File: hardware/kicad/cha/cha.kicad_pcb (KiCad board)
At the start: 4 copper layers, 173 x 134 mm, 138 parts, among them J1 AES_CHA, J2 PROG C, J3 PROG SM, J4 microSD, J5 Câble PROG-CHA, SW1 Retour menu, U1 AMS1117-3.3, U10 74AHCT1G32, U11 74LVC1G07, U12 iCE40HX4K-TQ144, U13 W25Q32JVSS, U14 AS4C32M16SB-6TIN, U15 iCE40HX4K-TQ144, U16 W25Q32JVSS, U17 IS61WV10248EDBLL-10TLI, U2 AP2112K-1.2, U3 74LVC16244A, U4 74LVC16244A, U5 74LVC16244A, U6 74LVC16244A, U7 74AHCT16244, U8 74AHCT16244, U9 74AHCT244, X1 25 MHz 3,3 V, X2 25 MHz 3,3 V

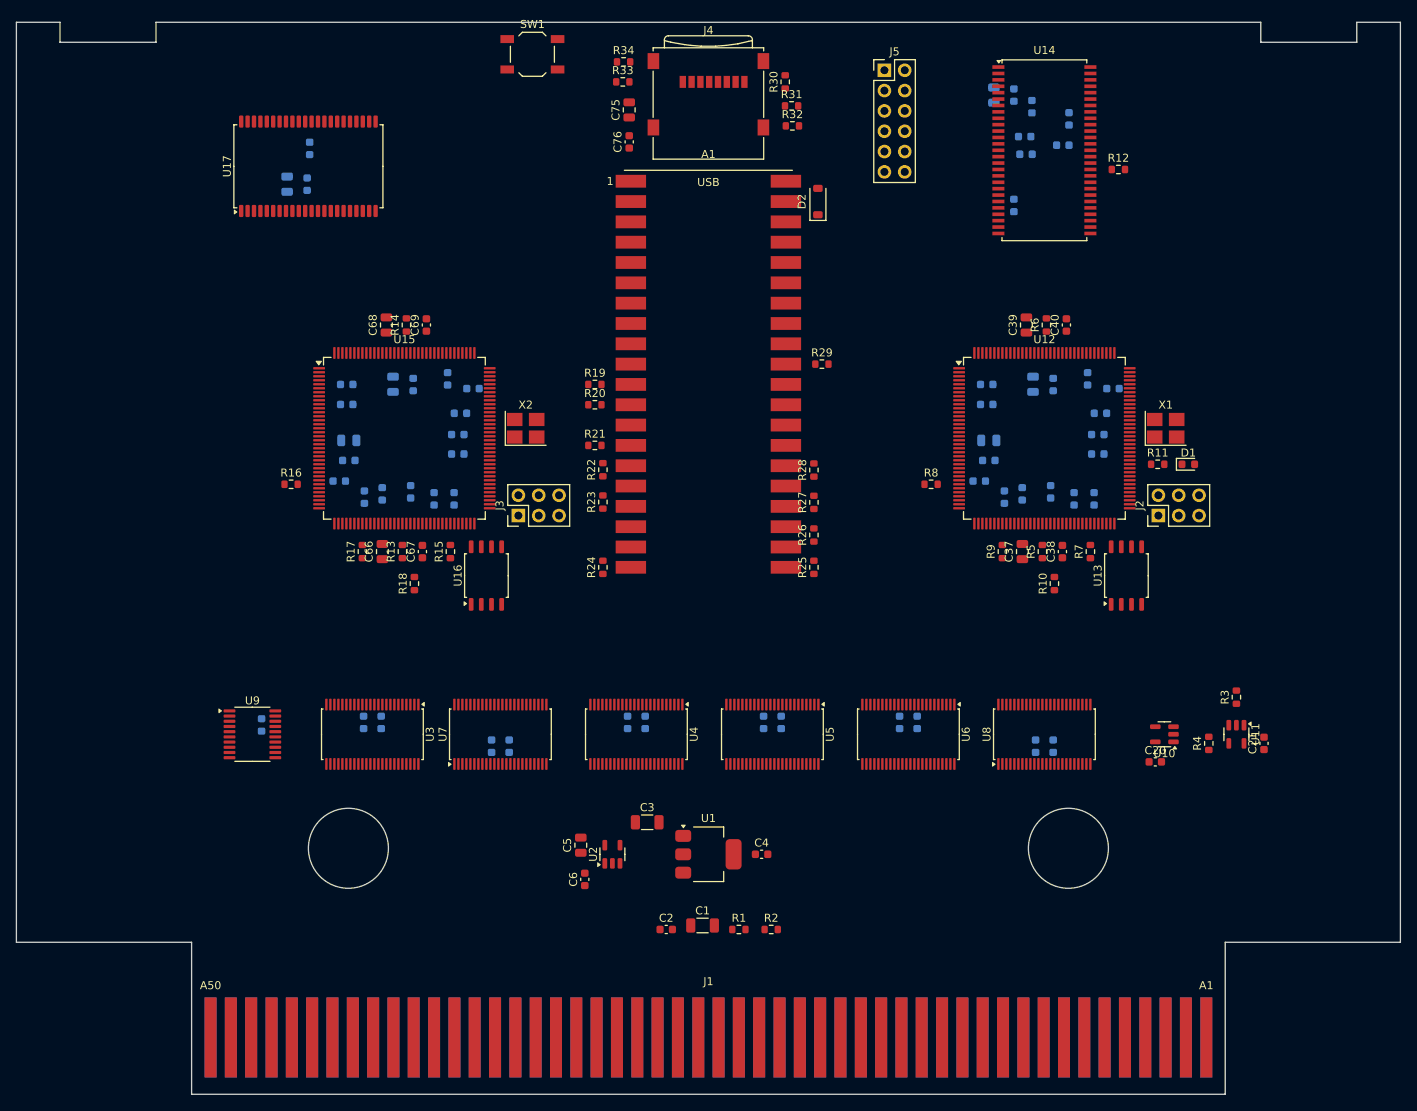
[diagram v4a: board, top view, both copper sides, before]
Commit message: PCB : 9 trous d'entretoise, vias vers les plans, zones interdites
- 9 trous M3 aux mêmes coordonnées sur PROG et CHA (H1-H9) pour relier
  les deux cartes par des entretoises ; 3,5 mm sans composant ni cuivre
  autour.
- Vias de raccordement aux plans (masse, +3V3) posés avant le routage
  pour chaque pastille CMS : au premier routage complet de la carte
  PROG, tous les signaux étaient routés et les 85 liaisons manquantes
  étaient toutes des raccordements aux plans.
- Zones interdites aux pistes autour des trous de la coque et des
  entretoises ; rétrécissement à 0,09 mm admis à l'entrée des broches.
- route.py : DRC par le module pcbnew (kicad-cli 7 n'en a pas), lecture
  de session corrigée.
- Pico descendu de 3 mm (chevauchait le lecteur microSD).

Co-Authored-By: Claude Opus 5.5 <noreply@anthropic.com>
Claude-Session: https://claude.ai/code/session_01WKfXP1YJ8otGxZ5dsY6Agh
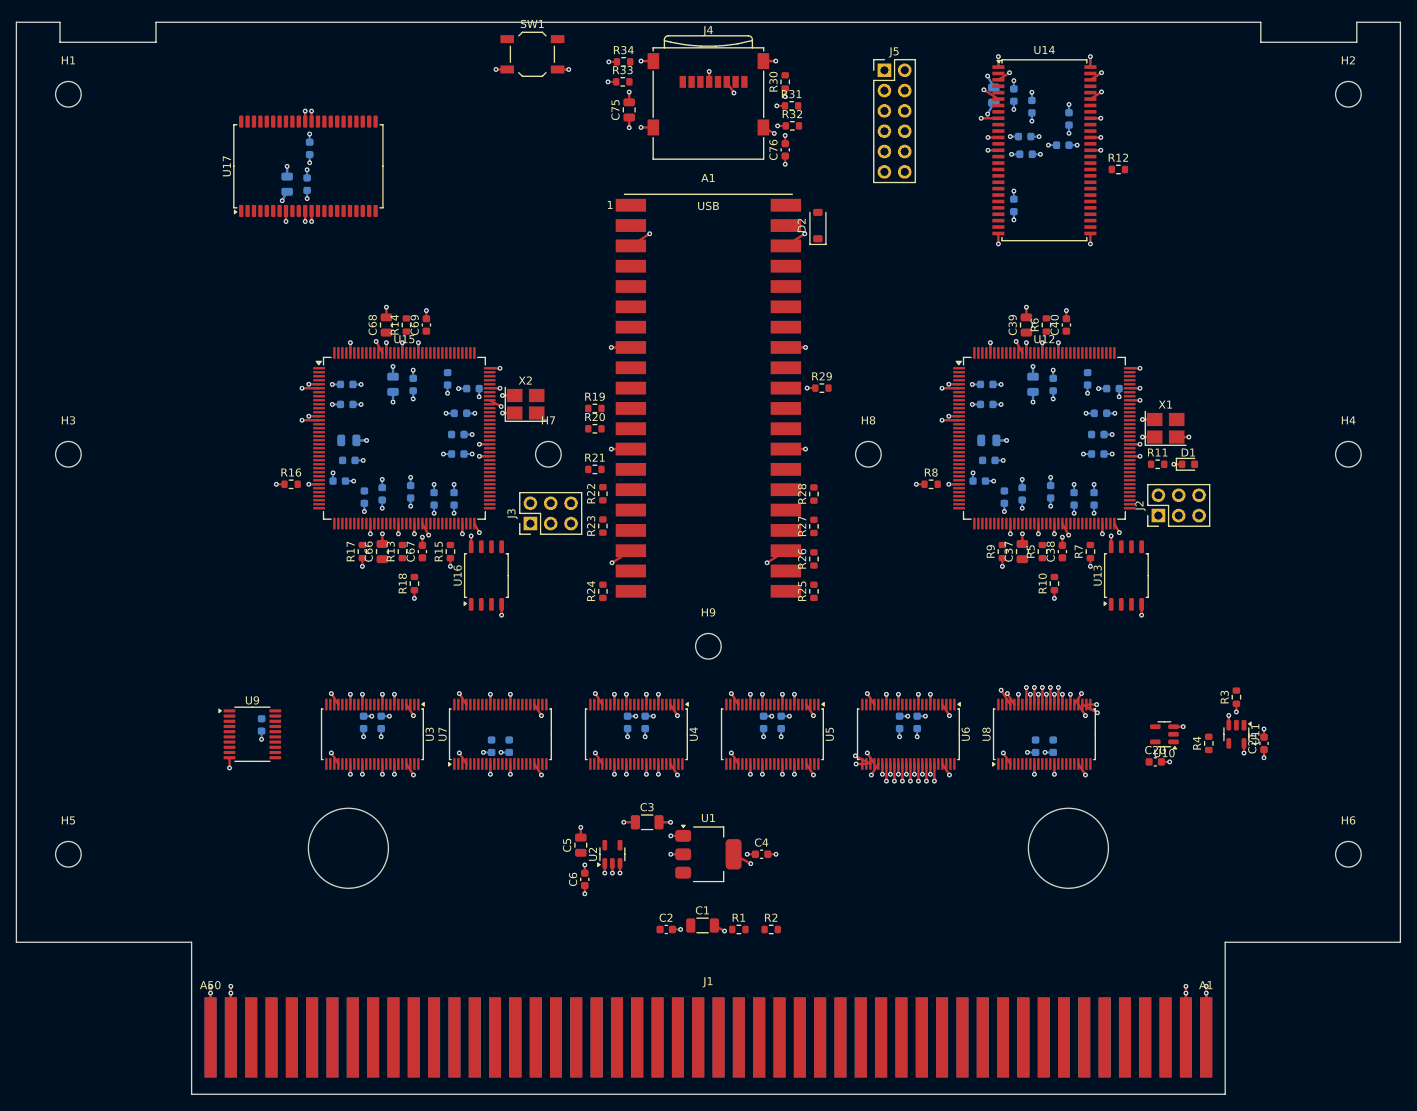
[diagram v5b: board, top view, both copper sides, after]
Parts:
- added H1: Entretoise M3, MountingHole:MountingHole_3.2mm_M3, F.Cu at (70.0, 55.0)
- added H2: Entretoise M3, MountingHole:MountingHole_3.2mm_M3, F.Cu at (230.0, 55.0)
- added H3: Entretoise M3, MountingHole:MountingHole_3.2mm_M3, F.Cu at (70.0, 100.0)
- added H4: Entretoise M3, MountingHole:MountingHole_3.2mm_M3, F.Cu at (230.0, 100.0)
- added H5: Entretoise M3, MountingHole:MountingHole_3.2mm_M3, F.Cu at (70.0, 150.0)
- added H6: Entretoise M3, MountingHole:MountingHole_3.2mm_M3, F.Cu at (230.0, 150.0)
- added H7: Entretoise M3, MountingHole:MountingHole_3.2mm_M3, F.Cu at (130.0, 100.0)
- added H8: Entretoise M3, MountingHole:MountingHole_3.2mm_M3, F.Cu at (170.0, 100.0)
- added H9: Entretoise M3, MountingHole:MountingHole_3.2mm_M3, F.Cu at (150.0, 124.0)
- moved C76 19.5 mm to (159.6, 62.0)
- moved A1 3.00 mm to (150.0, 93.0)
- moved D2 3.00 mm to (163.7, 71.4)
- moved R19 3.00 mm to (135.8, 94.3)
- moved R20 3.00 mm to (135.8, 96.8)
- moved R21 3.00 mm to (135.8, 101.9)
- moved R22 3.00 mm to (136.8, 104.9)
- moved R23 3.00 mm to (136.8, 109.0)
- moved R24 3.00 mm to (136.8, 117.1)
- moved R25 3.00 mm to (163.2, 117.1)
- moved R26 3.00 mm to (163.2, 113.1)
- moved R27 3.00 mm to (163.2, 109.0)
- moved R28 3.00 mm to (163.2, 105.0)
- moved R29 3.00 mm to (164.2, 91.7)
- moved X2 3.00 mm to (127.2, 93.8)
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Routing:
- net GND: track 0.00 -> 336.5 mm, vias 0 -> 215
- net +3V3: track 0.00 -> 147.9 mm, vias 0 -> 121

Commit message: FPGA configurés par le RP2350 depuis la carte SD (plus de flash)
- Matériel : flash SPI retirées (4 W25Q32, 12 résistances, 4
  condensateurs). Le bus de liaison arrive sur les broches de
  configuration des iCE40 (LK_SCK -> 70 SCK, LK_IO[0] -> 68 SDI,
  LK_CS_N -> 71 SS), qui redeviennent ces entrées après le démarrage.
  CRESET_N commun aux 4 FPGA, tiré à la masse, piloté par le RP2350
  (GP28) ; câble PROG-CHA en 2 x 7 (CRESET_N + masse). Connecteur 2 x 3
  de secours par FPGA (iceprog -S).
- Firmware : fpga_boot.c (reset commun en mode SPI esclave, envoi des
  SDAES/fpga_*.bin l'un après l'autre, contrôle de CDONE) ; testé sur
  PC (bitstreams reçus à l'identique, FPGA laissés en reset si un
  fichier manque).
- make -C hdl sd : fichiers à copier sur la carte SD.
- PCB : table de placement et références des FPGA mises à jour,
  broches réoptimisées.
Placement-routage des FPGA avec les nouvelles broches : en cours.

Co-Authored-By: Claude Opus 5.5 <noreply@anthropic.com>
Claude-Session: https://claude.ai/code/session_01WKfXP1YJ8otGxZ5dsY6Agh
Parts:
- removed C75: 10u, Capacitor_SMD:C_0805_2012Metric
- removed C76: 100n, Capacitor_SMD:C_0603_1608Metric
- removed R29, R30, R31, R32, R33, R34: 10k, Resistor_SMD:R_0603_1608Metric
- removed U16: W25Q32JVSS, Package_SO:SOIC-8_5.23x5.23mm_P1.27mm
- removed U17: IS61WV10248EDBLL-10TLI, Package_SO:TSOP-II-44_10.16x18.41mm_P0.8mm
- C49, C54, C64, C67, C72: value 100n -> 10u; footprint Capacitor_SMD:C_0603_1608Metric -> Capacitor_SMD:C_0805_2012Metric
- C50, C55, C66, C68: value 10u -> 100n; footprint Capacitor_SMD:C_0805_2012Metric -> Capacitor_SMD:C_0603_1608Metric
- C65: moved to F.Cu
- C69: moved to B.Cu
- C73: value 100n -> 10u; footprint Capacitor_SMD:C_0603_1608Metric -> Capacitor_SMD:C_0805_2012Metric; moved to F.Cu
- C74: value 10u -> 100n; footprint Capacitor_SMD:C_0805_2012Metric -> Capacitor_SMD:C_0603_1608Metric; moved to F.Cu
- J2: value PROG C -> CONF C
- J3: value PROG SM -> CONF SM
- J5: footprint Connector_PinHeader_2.54mm:PinHeader_2x06_P2.54mm_Vertical -> Connector_PinHeader_2.54mm:PinHeader_2x07_P2.54mm_Vertical
- R10: value 10k -> 100
- R11: value 470 -> 100
- R12, R23, R24, R25, R26, R27, R28: value 33 -> 10k
- R13, R14: value 100 -> 33
- R15, R16, R17, R18, R9: value 10k -> 33
- R8: value 10k -> 470
- U13: value W25Q32JVSS -> AS4C32M16SB-6TIN; footprint Package_SO:SOIC-8_5.23x5.23mm_P1.27mm -> Package_SO:TSOP-II-54_22.2x10.16mm_P0.8mm
- U14: value AS4C32M16SB-6TIN -> iCE40HX4K-TQ144; footprint Package_SO:TSOP-II-54_22.2x10.16mm_P0.8mm -> Package_QFP:TQFP-144_20x20mm_P0.5mm
- U15: value iCE40HX4K-TQ144 -> IS61WV10248EDBLL-10TLI; footprint Package_QFP:TQFP-144_20x20mm_P0.5mm -> Package_SO:TSOP-II-44_10.16x18.41mm_P0.8mm
- moved R12 96.2 mm to (117.8, 112.2), turned to 90 degrees
- moved R11 95.5 mm to (112.2, 83.8), turned to 90 degrees
- moved C50 92.7 mm to (105.1, 100.8), turned to 0 degrees
- moved U14 87.7 mm to (112.0, 98.0)
- moved R10 81.6 mm to (111.8, 112.2)
- moved R24 67.6 mm to (159.6, 53.5)
- moved C74 62.4 mm to (159.6, 62.0), turned to 90 degrees
- moved R25 60.7 mm to (160.4, 56.5), turned to 0 degrees
- moved R27 60.5 mm to (139.3, 53.5), turned to 0 degrees
- moved R28 59.0 mm to (139.4, 51.0), turned to 0 degrees
- moved R26 54.2 mm to (160.5, 59.0), turned to 0 degrees
- moved U13 54.1 mm to (192.0, 62.0), turned to 0 degrees
- moved C42 51.0 mm to (188.2, 55.1)
- moved R9 49.9 mm to (201.2, 64.4), turned to 0 degrees
- moved C71 46.5 mm to (100.2, 61.8)
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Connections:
- A1 pad 34: (no net) -> CRESET_N
- C50 pad 1: +3V3 -> +1V2
- C55 pad 1: +1V2 -> +3V3
- C65 pad 1: +3V3 -> SM_VCCPLL0
- C67 pad 1: SM_VCCPLL0 -> SM_VCCPLL1
- C69 pad 1: SM_VCCPLL1 -> +3V3
- J2 pad 1: C_FL_SCK -> CHA_SCK
- J2 pad 2: C_FL_CS_N -> CS_C
- J2 pad 3: C_FL_DI -> C_SDO
- J2 pad 4: C_FL_DO -> CHA_IO0
- J2 pad 5: C_CRESET_N -> CRESET_N
- J3 pad 1: SM_FL_SCK -> CHA_SCK
- J3 pad 2: SM_FL_CS_N -> CS_SM
- J3 pad 3: SM_FL_DI -> SM_SDO
- J3 pad 4: SM_FL_DO -> CHA_IO0
- J3 pad 5: SM_CRESET_N -> CRESET_N
- R10 pad 1: +3V3 -> +1V2
- R10 pad 2: C_FL_HOLD_N -> SM_VCCPLL0
- R11 pad 1: C_LED -> +1V2
- R11 pad 2: C_LED_K -> SM_VCCPLL1
- R12 pad 1: C_SD_CLK -> CRESET_N
- R12 pad 2: C_SD_CLK_R -> GND
- R13 pad 1: +1V2 -> PROG_SCK_MCU
- R13 pad 2: SM_VCCPLL0 -> PROG_SCK
- R14 pad 1: +1V2 -> PROG_IO0_MCU
- R14 pad 2: SM_VCCPLL1 -> PROG_IO0
- R15 pad 1: +3V3 -> PROG_IO1_MCU
- R15 pad 2: SM_CRESET_N -> PROG_IO1
- R16 pad 1: +3V3 -> PROG_IO2_MCU
- R16 pad 2: SM_FL_CS_N -> PROG_IO2
- R17 pad 1: +3V3 -> PROG_IO3_MCU
- R17 pad 2: SM_FL_WP_N -> PROG_IO3
- R18 pad 1: +3V3 -> CHA_SCK_MCU
- R18 pad 2: SM_FL_HOLD_N -> CHA_SCK
- R19 pad 1: PROG_SCK_MCU -> CHA_IO0_MCU
- R19 pad 2: PROG_SCK -> CHA_IO0
- R20 pad 1: PROG_IO0_MCU -> CHA_IO1_MCU
- R20 pad 2: PROG_IO0 -> CHA_IO1
- R21 pad 1: PROG_IO1_MCU -> CHA_IO2_MCU
- R21 pad 2: PROG_IO1 -> CHA_IO2
- R22 pad 1: PROG_IO2_MCU -> CHA_IO3_MCU
- R22 pad 2: PROG_IO2 -> CHA_IO3
- R23 pad 1: PROG_IO3_MCU -> +3V3
- R23 pad 2: PROG_IO3 -> CDONE
- R24 pad 1: CHA_SCK_MCU -> +3V3
- R24 pad 2: CHA_SCK -> SD_CMD
- R25 pad 1: CHA_IO0_MCU -> +3V3
- R25 pad 2: CHA_IO0 -> SD_D0
- R26 pad 1: CHA_IO1_MCU -> +3V3
- R26 pad 2: CHA_IO1 -> SD_D1
- R27 pad 1: CHA_IO2_MCU -> +3V3
- R27 pad 2: CHA_IO2 -> SD_D2
- R28 pad 1: CHA_IO3_MCU -> +3V3
- R28 pad 2: CHA_IO3 -> SD_D3
- R7 pad 1: +3V3 -> CRESET_N
- R7 pad 2: C_CRESET_N -> GND
- R8 pad 1: +3V3 -> C_LED
- R8 pad 2: C_FL_CS_N -> C_LED_K
- R9 pad 1: +3V3 -> C_SD_CLK
- R9 pad 2: C_FL_WP_N -> C_SD_CLK_R
- U12 pad 1: CHA_IO3 -> MODE
- U12 pad 10: P1 -> P2
- U12 pad 101: C_SD_A11 -> C_SD_A9
- U12 pad 102: C_SD_A12 -> C_SD_A11
- U12 pad 104: C_SD_CKE -> C_SD_A12
- U12 pad 105: C_SD_DQM1 -> C_SD_CKE
- U12 pad 106: C_SD_DQ8 -> C_SD_DQM1
- U12 pad 107: C_SD_DQ9 -> C_SD_DQ8
- U12 pad 11: P2 -> P3
- U12 pad 110: C_SD_DQ10 -> C_SD_DQ9
- U12 pad 112: C_SD_DQ11 -> C_SD_DQ10
- U12 pad 113: C_SD_DQ12 -> C_SD_DQ11
- U12 pad 114: C_SD_DQ13 -> C_SD_DQ12
- U12 pad 115: C_SD_DQ14 -> C_SD_DQ13
- U12 pad 116: C_SD_DQ15 -> C_SD_DQ14
- U12 pad 117: C_SD_DQ0 -> C_SD_DQ15
- U12 pad 118: C_SD_DQ1 -> C_SD_DQ0
- U12 pad 119: C_SD_DQ2 -> C_SD_DQ1
- U12 pad 12: P3 -> P12
- U12 pad 120: C_SD_DQ3 -> C_SD_DQ2
- U12 pad 121: C_SD_DQ4 -> C_SD_DQ3
- U12 pad 122: C_SD_DQ5 -> C_SD_DQ4
- U12 pad 124: C_SD_DQ6 -> C_SD_DQ5
- U12 pad 125: C_SD_DQ7 -> C_SD_DQ6
- U12 pad 128: C_SD_DQM0 -> C_SD_DQ7
- U12 pad 129: C_SD_WE_N -> C_SD_DQM0
- U12 pad 130: C_SD_CAS_N -> C_SD_WE_N
- U12 pad 134: C_SD_RAS_N -> C_SD_CAS_N
- U12 pad 135: C_SD_CS_N -> C_SD_RAS_N
- U12 pad 136: C_SD_BA0 -> C_SD_CS_N
- U12 pad 137: C_SD_BA1 -> C_SD_BA0
- U12 pad 138: C_SD_A10 -> C_SD_BA1
- U12 pad 139: C_SD_A0 -> C_SD_A10
- U12 pad 141: C_SD_A1 -> C_SD_A0
- U12 pad 142: C_SD_A2 -> C_SD_A1
- U12 pad 143: C_SD_A3 -> C_SD_A2
- U12 pad 144: MODE -> C_SD_A3
- U12 pad 15: P12 -> P13
- U12 pad 16: P10 -> P4
- U12 pad 17: P13 -> P5
- U12 pad 18: P4 -> P14
- U12 pad 19: P5 -> P15
- U12 pad 2: CHA_IO2 -> CHA_IO3
- U12 pad 22: P14 -> P6
- U12 pad 23: P15 -> P8
- U12 pad 24: P6 -> P7
- U12 pad 25: P7 -> P9
- U12 pad 26: P8 -> P11
- U12 pad 28: P9 -> GBD3
- U12 pad 29: P11 -> GBD2
- U12 pad 3: CHA_IO1 -> CHA_IO2
- U12 pad 31: GBD3 -> GBD1
- U12 pad 32: GBD2 -> GBD0
- U12 pad 33: GBD1 -> GAD3
- U12 pad 34: GBD0 -> GAD2
- U12 pad 37: GAD3 -> GAD1
- U12 pad 38: GAD2 -> GAD0
- U12 pad 39: GAD1 -> DOTB
- U12 pad 4: CHA_SCK -> CHA_IO1
- U12 pad 41: GAD0 -> DOTA
- U12 pad 42: DOTB -> P17
- U12 pad 43: DOTA -> P16
- U12 pad 44: P17 -> P19
- U12 pad 45: P16 -> P18
- U12 pad 47: P19 -> P21
- U12 pad 48: P18 -> P20
- U12 pad 49: P21 -> P23
- U12 pad 52: P20 -> P22
- U12 pad 55: P23 -> XLAT_EN_N
- U12 pad 56: P22 -> EVEN
- U12 pad 60: XLAT_EN_N -> H
- U12 pad 61: EVEN -> LOAD
- U12 pad 62: H -> CA4
- U12 pad 63: LOAD -> (no net)
- U12 pad 64: CA4 -> (no net)
- U12 pad 66: C_CRESET_N -> CRESET_N
- U12 pad 67: C_FL_DI -> C_SDO
- U12 pad 68: C_FL_DO -> CHA_IO0
- U12 pad 7: CHA_IO0 -> P0
- U12 pad 70: C_FL_SCK -> CHA_SCK
- U12 pad 71: C_FL_CS_N -> CS_C
- U12 pad 8: CS_C -> P1
- U12 pad 84: C_LED -> (no net)
- U12 pad 87: (no net) -> C_LED
- U12 pad 9: P0 -> P10
- U12 pad 91: C_SD_CLK -> (no net)
- U12 pad 94: C_SD_A4 -> C_SD_CLK
- U12 pad 95: C_SD_A5 -> C_SD_A4
- U12 pad 96: C_SD_A6 -> C_SD_A5
- U12 pad 97: C_SD_A7 -> C_SD_A6
- U12 pad 98: C_SD_A8 -> C_SD_A7
- U12 pad 99: C_SD_A9 -> C_SD_A8
- U13 pad 1: C_FL_CS_N -> +3V3
- U13 pad 2: C_FL_DO -> C_SD_DQ0
- U13 pad 3: C_FL_WP_N -> +3V3
- U13 pad 4: GND -> C_SD_DQ1
- U13 pad 5: C_FL_DI -> C_SD_DQ2
- U13 pad 6: C_FL_SCK -> GND
- U13 pad 7: C_FL_HOLD_N -> C_SD_DQ3
- U13 pad 8: +3V3 -> C_SD_DQ4
- U14 pad 1: +3V3 -> SR_A18
- U14 pad 10: C_SD_DQ5 -> SR_A0
- U14 pad 11: C_SD_DQ6 -> (no net)
- U14 pad 12: GND -> (no net)
- U14 pad 13: C_SD_DQ7 -> GND
- U14 pad 14: +3V3 -> GND
- U14 pad 15: C_SD_DQM0 -> (no net)
- U14 pad 16: C_SD_WE_N -> (no net)
- U14 pad 17: C_SD_CAS_N -> (no net)
- U14 pad 18: C_SD_RAS_N -> (no net)
- U14 pad 19: C_SD_CS_N -> (no net)
- U14 pad 2: C_SD_DQ0 -> SR_D1
- U14 pad 20: C_SD_BA0 -> PCK2B
- U14 pad 21: C_SD_BA1 -> (no net)
- U14 pad 22: C_SD_A10 -> (no net)
- U14 pad 23: C_SD_A0 -> SDD0
- U14 pad 24: C_SD_A1 -> SDD1
- U14 pad 25: C_SD_A2 -> SDD2
- U14 pad 26: C_SD_A3 -> SDD3
- U14 pad 27: +3V3 -> +1V2
- U14 pad 28: GND -> SDD4
- U14 pad 29: C_SD_A4 -> SDD5
- U14 pad 3: +3V3 -> SR_D0
- U14 pad 30: C_SD_A5 -> +3V3
- U14 pad 31: C_SD_A6 -> SDD6
- U14 pad 32: C_SD_A7 -> SDD7
- U14 pad 33: C_SD_A8 -> SDA2
- U14 pad 34: C_SD_A9 -> SDA3
- U14 pad 35: C_SD_A11 -> (no net)
- U14 pad 36: C_SD_A12 -> (no net)
- U14 pad 37: C_SD_CKE -> SDA4
- U14 pad 38: C_SD_CLK_R -> SDA5
- U14 pad 39: C_SD_DQM1 -> SDA6
- U14 pad 4: C_SD_DQ1 -> SR_A4
- U14 pad 40: (no net) -> +1V2
- U14 pad 41: GND -> SDA7
- U14 pad 42: C_SD_DQ8 -> SDA8
- U14 pad 43: +3V3 -> SDA9
- U14 pad 44: C_SD_DQ9 -> SDA10
- U14 pad 45: C_SD_DQ10 -> SDA11
- U14 pad 46: GND -> +3V3
- U14 pad 47: C_SD_DQ11 -> SDA12
- U14 pad 48: C_SD_DQ12 -> SDA13
- U14 pad 49: +3V3 -> SDA14
- U14 pad 5: C_SD_DQ2 -> GND
- U14 pad 50: C_SD_DQ13 -> (no net)
- U14 pad 51: C_SD_DQ14 -> (no net)
- U14 pad 52: GND -> SDA15
- U14 pad 53: C_SD_DQ15 -> GND
- U14 pad 54: GND -> SM_VCCPLL0
- U14 pad 6: GND -> +3V3
- U14 pad 7: C_SD_DQ3 -> SR_A3
- U14 pad 8: C_SD_DQ4 -> SR_A2
- U14 pad 9: +3V3 -> SR_A1
- U15 pad 1: SR_A18 -> (no net)
- U15 pad 10: SR_A0 -> SR_D1
- U15 pad 11: (no net) -> +3V3
- U15 pad 12: (no net) -> GND
- U15 pad 13: GND -> SR_D2
- U15 pad 14: GND -> SR_D3
- U15 pad 15: (no net) -> SR_WE_N
- U15 pad 16: (no net) -> SR_A5
- U15 pad 17: (no net) -> SR_A6
- U15 pad 18: (no net) -> SR_A7
- U15 pad 19: (no net) -> SR_A8
- U15 pad 2: SR_D1 -> (no net)
- U15 pad 20: PCK2B -> SR_A9
- U15 pad 22: SDD0 -> (no net)
- U15 pad 23: SDD1 -> (no net)
- U15 pad 24: SDD2 -> (no net)
- U15 pad 25: SDD3 -> SR_A19
- U15 pad 26: SDD4 -> SR_A10
- U15 pad 27: +1V2 -> SR_A11
- U15 pad 28: SDD5 -> SR_A12
- U15 pad 29: SDD6 -> SR_A13
- U15 pad 3: SR_D0 -> SR_A0
- U15 pad 30: +3V3 -> SR_A14
- U15 pad 31: SDD7 -> SR_D4
- U15 pad 32: SDA2 -> SR_D5
- U15 pad 33: SDA3 -> +3V3
- U15 pad 34: SDA4 -> GND
- U15 pad 35: (no net) -> SR_D6
- U15 pad 36: (no net) -> SR_D7
- U15 pad 37: SDA5 -> SR_OE_N
- U15 pad 38: SDA6 -> SR_A15
- U15 pad 39: SDA7 -> SR_A16
- U15 pad 4: SR_A4 -> SR_A1
- U15 pad 40: +1V2 -> SR_A17
- U15 pad 41: SDA8 -> SR_A18
- U15 pad 42: SDA9 -> (no net)
- U15 pad 43: SDA10 -> (no net)
- U15 pad 44: SDA11 -> (no net)
- U15 pad 5: GND -> SR_A2
- U15 pad 6: +3V3 -> SR_A3
- U15 pad 7: SR_A3 -> SR_A4
- U15 pad 8: SR_A2 -> GND
- U15 pad 9: SR_A1 -> SR_D0
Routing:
- net +3V3: track 147.9 -> 135.0 mm, vias 121 -> 109
- net GND: track 336.5 -> 333.8 mm, vias 215 -> 213
